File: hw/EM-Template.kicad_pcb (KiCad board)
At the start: 2 copper layers, 100 x 100 mm, 0 parts

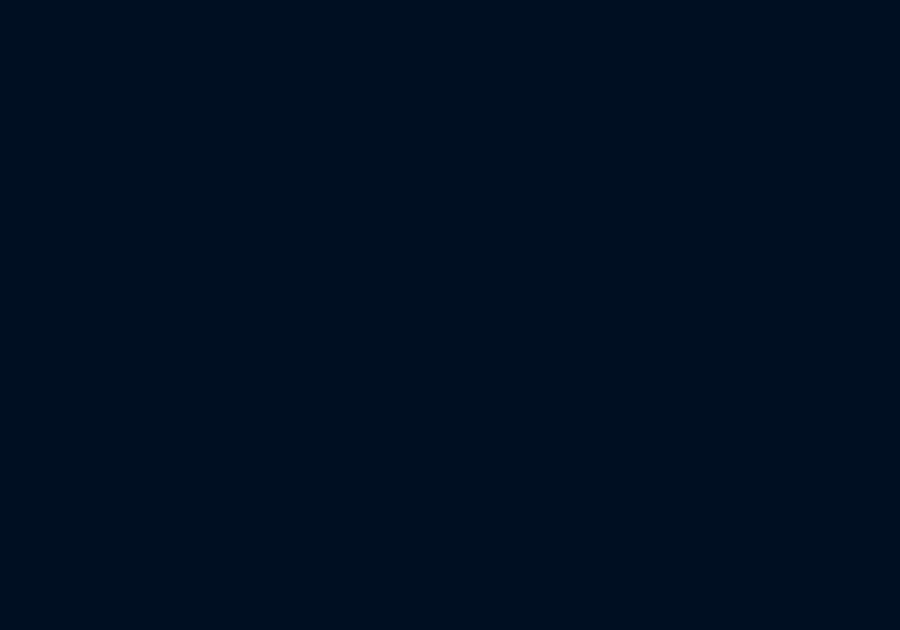
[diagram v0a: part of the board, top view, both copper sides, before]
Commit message: Add git SHA to PCB
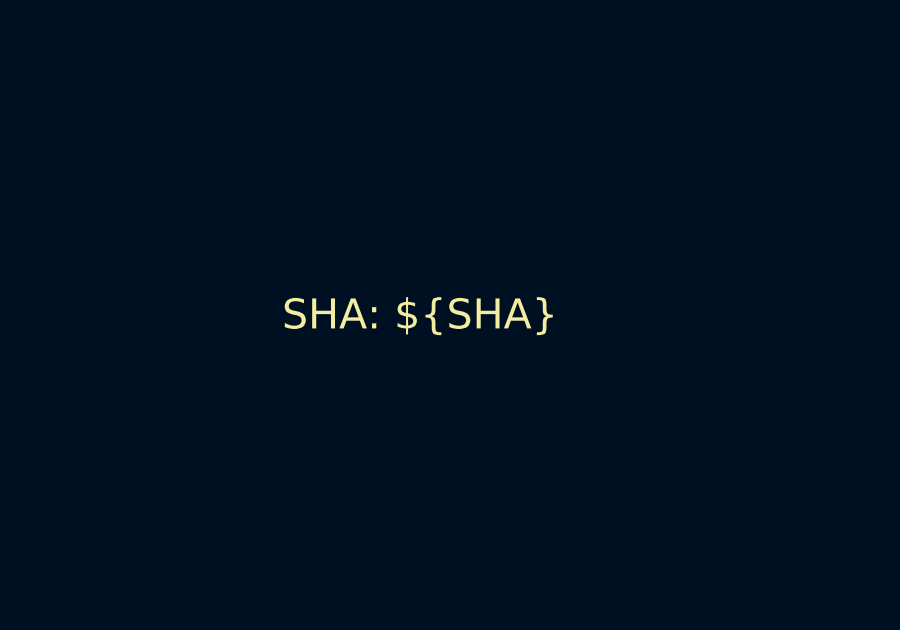
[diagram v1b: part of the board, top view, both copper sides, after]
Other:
- board text added: "SHA: ${SHA}"
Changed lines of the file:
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@@
     )
   )
+  (property "SHA" "#######")
   (net 0 "")
   (gr_rect (start 100 50) (end 200 150)
     (stroke (width 0.1) (type default)) (fill none) (layer "Edge.Cuts"))
+  (gr_text "SHA: ${SHA}" (at 145 115) (layer "F.SilkS")
+    (effects (font (size 1 1) (thickness 0.15)) (justify left bottom))
+  )
 )

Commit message: Changed template to use text variables
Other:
- board outline removed
- board text removed: "SHA: ${SHA}"
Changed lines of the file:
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@@
-(kicad_pcb (version 20221018) (generator pcbnew)
-  (general
-    (thickness 1.6)
-  )
-  (paper "A4")
-  (title_block
-    (title "EM-Template")
-    (rev "1.0")
-  )
-  (layers
-    (0 "F.Cu" signal)
-    (31 "B.Cu" signal)
-    (32 "B.Adhes" user "B.Adhesive")
-    (33 "F.Adhes" user "F.Adhesive")
-    (34 "B.Paste" user)
-    (35 "F.Paste" user)
-    (36 "B.SilkS" user "B.Silkscreen")
-    (37 "F.SilkS" user "F.Silkscreen")
-    (38 "B.Mask" user)
-    (39 "F.Mask" user)
-    (40 "Dwgs.User" user "User.Drawings")
-    (41 "Cmts.User" user "User.Comments")
-    (42 "Eco1.User" user "User.Eco1")
-    (43 "Eco2.User" user "User.Eco2")
-    (44 "Edge.Cuts" user)
-    (45 "Margin" user)
-    (46 "B.CrtYd" user "B.Courtyard")
-    (47 "F.CrtYd" user "F.Courtyard")
-    (48 "B.Fab" user)
-    (49 "F.Fab" user)
-    (50 "User.1" user)
-    (51 "User.2" user)
-    (52 "User.3" user)
-    (53 "User.4" user)
-    (54 "User.5" user)
-    (55 "User.6" user)
-    (56 "User.7" user)
-    (57 "User.8" user)
-    (58 "User.9" user)
-  )
-  (setup
-    (stackup
-      (layer "F.SilkS" (type "Top Silk Screen") (color "White"))
-      (layer "F.Paste" (type "Top Solder Paste"))
-      (layer "F.Mask" (type "Top Solder Mask") (color "Red") (thickness 0.01))
-      (layer "F.Cu" (type "copper") (thickness 0.035))
-      (layer "dielectric 1" (type "core") (color "FR4 natural") (thickness 1.51) (material "FR4") (epsilon_r 4.5) (loss_tangent 0.02))
-      (layer "B.Cu" (type "copper") (thickness 0.035))
-      (layer "B.Mask" (type "Bottom Solder Mask") (color "Red") (thickness 0.01))
-      (layer "B.Paste" (type "Bottom Solder Paste"))
-      (layer "B.SilkS" (type "Bottom Silk Screen") (color "White"))
-      (copper_finish "HAL SnPb")
-      (dielectric_constraints no)
-    )
-    (pad_to_mask_clearance 0)
-    (pcbplotparams
-      (layerselection 0x00010fc_ffffffff)
-      (plot_on_all_layers_selection 0x0000000_00000000)
-      (disableapertmacros false)
-      (usegerberextensions false)
-      (usegerberattributes true)
-      (usegerberadvancedattributes true)
-      (creategerberjobfile true)
-      (dashed_line_dash_ratio 12.000000)
-      (dashed_line_gap_ratio 3.000000)
-      (svgprecision 4)
-      (plotframeref false)
-      (viasonmask false)
-      (mode 1)
-      (useauxorigin false)
-      (hpglpennumber 1)
-      (hpglpenspeed 20)
-      (hpglpendiameter 15.000000)
-      (dxfpolygonmode true)
-      (dxfimperialunits true)
-      (dxfusepcbnewfont true)
-      (psnegative false)
-      (psa4output false)
-      (plotreference true)
-      (plotvalue true)
-      (plotinvisibletext false)
-      (sketchpadsonfab false)
-      (subtractmaskfromsilk false)
-      (outputformat 1)
-      (mirror false)
-      (drillshape 1)
-      (scaleselection 1)
-      (outputdirectory "")
-    )
-  )
-  (property "SHA" "#######")
-  (net 0 "")
-  (gr_rect (start 100 50) (end 200 150)
-    (stroke (width 0.1) (type default)) (fill none) (layer "Edge.Cuts"))
-  (gr_text "SHA: ${SHA}" (at 145 115) (layer "F.SilkS")
-    (effects (font (size 1 1) (thickness 0.15)) (justify left bottom))
-  )
+(kicad_pcb
+	(version 20241229)
+	(generator "pcbnew")
+	(generator_version "9.0")
+	(general
+		(thickness 1.6)
+		(legacy_teardrops no)
+	)
+	(paper "A4")
+	(title_block
+		(title "EM-Template")
+		(date "${date}")
+		(rev "${rev}")
+		(company "Dolvac Instruments")
+		(comment 1 "SHA: ${sha}")
+	)
+	(layers
+		(0 "F.Cu" signal)
+		(2 "B.Cu" signal)
+		(9 "F.Adhes" user "F.Adhesive")
+		(11 "B.Adhes" user "B.Adhesive")
+		(13 "F.Paste" user)
+		(15 "B.Paste" user)
+		(5 "F.SilkS" user "F.Silkscreen")
+		(7 "B.SilkS" user "B.Silkscreen")
+		(1 "F.Mask" user)
+		(3 "B.Mask" user)
+		(17 "Dwgs.User" user "User.Drawings")
+		(19 "Cmts.User" user "User.Comments")
+		(21 "Eco1.User" user "User.Eco1")
+		(23 "Eco2.User" user "User.Eco2")
+		(25 "Edge.Cuts" user)
+		(27 "Margin" user)
+		(31 "F.CrtYd" user "F.Courtyard")
+		(29 "B.CrtYd" user "B.Courtyard")
+		(35 "F.Fab" user)
+		(33 "B.Fab" user)
+		(39 "User.1" user)
+		(41 "User.2" user)
+		(43 "User.3" user)
+		(45 "User.4" user)
+		(47 "User.5" user)
+		(49 "User.6" user)
+		(51 "User.7" user)
+		(53 "User.8" user)
+		(55 "User.9" user)
+	)
+	(setup
+		(stackup
+			(layer "F.SilkS"
+				(type "Top Silk Screen")
+				(color "White")
+			)
+			(layer "F.Paste"
+				(type "Top Solder Paste")
+			)
+			(layer "F.Mask"
+				(type "Top Solder Mask")
+				(color "Red")
+				(thickness 0.01)
+			)
+			(layer "F.Cu"
+				(type "copper")
+				(thickness 0.035)
+			)
+			(layer "dielectric 1"
+				(type "core")
+				(color "FR4 natural")
+				(thickness 1.51)
+				(material "FR4")
+				(epsilon_r 4.5)
+				(loss_tangent 0.02)
+			)
+			(layer "B.Cu"
+				(type "copper")
+				(thickness 0.035)
+			)
+			(layer "B.Mask"
+				(type "Bottom Solder Mask")
+				(color "Red")
+				(thickness 0.01)
+			)
+			(layer "B.Paste"
+				(type "Bottom Solder Paste")
+			)
+			(layer "B.SilkS"
+				(type "Bottom Silk Screen")
+				(color "White")
+			)
+			(copper_finish "HAL SnPb")
+			(dielectric_constraints no)
+		)
+		(pad_to_mask_clearance 0)
+		(allow_soldermask_bridges_in_footprints no)
+		(tenting front back)
+		(pcbplotparams
+			(layerselection 0x00000000_00000000_55555555_5755f5ff)
+			(plot_on_all_layers_selection 0x00000000_00000000_00000000_00000000)
+			(disableapertmacros no)
+			(usegerberextensions no)
+			(usegerberattributes yes)
+			(usegerberadvancedattributes yes)
+			(creategerberjobfile yes)
+			(dashed_line_dash_ratio 12.000000)
+			(dashed_line_gap_ratio 3.000000)
+			(svgprecision 4)
+			(plotframeref no)
+			(mode 1)
+			(useauxorigin no)
+			(hpglpennumber 1)
+			(hpglpenspeed 20)
+			(hpglpendiameter 15.000000)
+			(pdf_front_fp_property_popups yes)
+			(pdf_back_fp_property_popups yes)
+			(pdf_metadata yes)
+			(pdf_single_document no)
+			(dxfpolygonmode yes)
+			(dxfimperialunits yes)
+			(dxfusepcbnewfont yes)
+			(psnegative no)
+			(psa4output no)
+			(plot_black_and_white yes)
+			(plotinvisibletext no)
+			(sketchpadsonfab no)
+			(plotpadnumbers no)
+			(hidednponfab no)
+			(sketchdnponfab yes)
+			(crossoutdnponfab yes)
+			(subtractmaskfromsilk no)
+			(outputformat 1)
+			(mirror no)
+			(drillshape 1)
+			(scaleselection 1)
+			(outputdirectory "")
+		)
+	)
+	(property "date" "0000-00-00")
+	(property "rev" "0.0")
+	(property "sha" "DEADBEEF")
+	(net 0 "")
+	(embedded_fonts no)
 )
